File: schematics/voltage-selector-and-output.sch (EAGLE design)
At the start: 24 parts, among them IC2 Tiny85-20-SMT, IC3 MCP41010P, IC4 5V, IC5 MIC2941, X1 USB-A-H

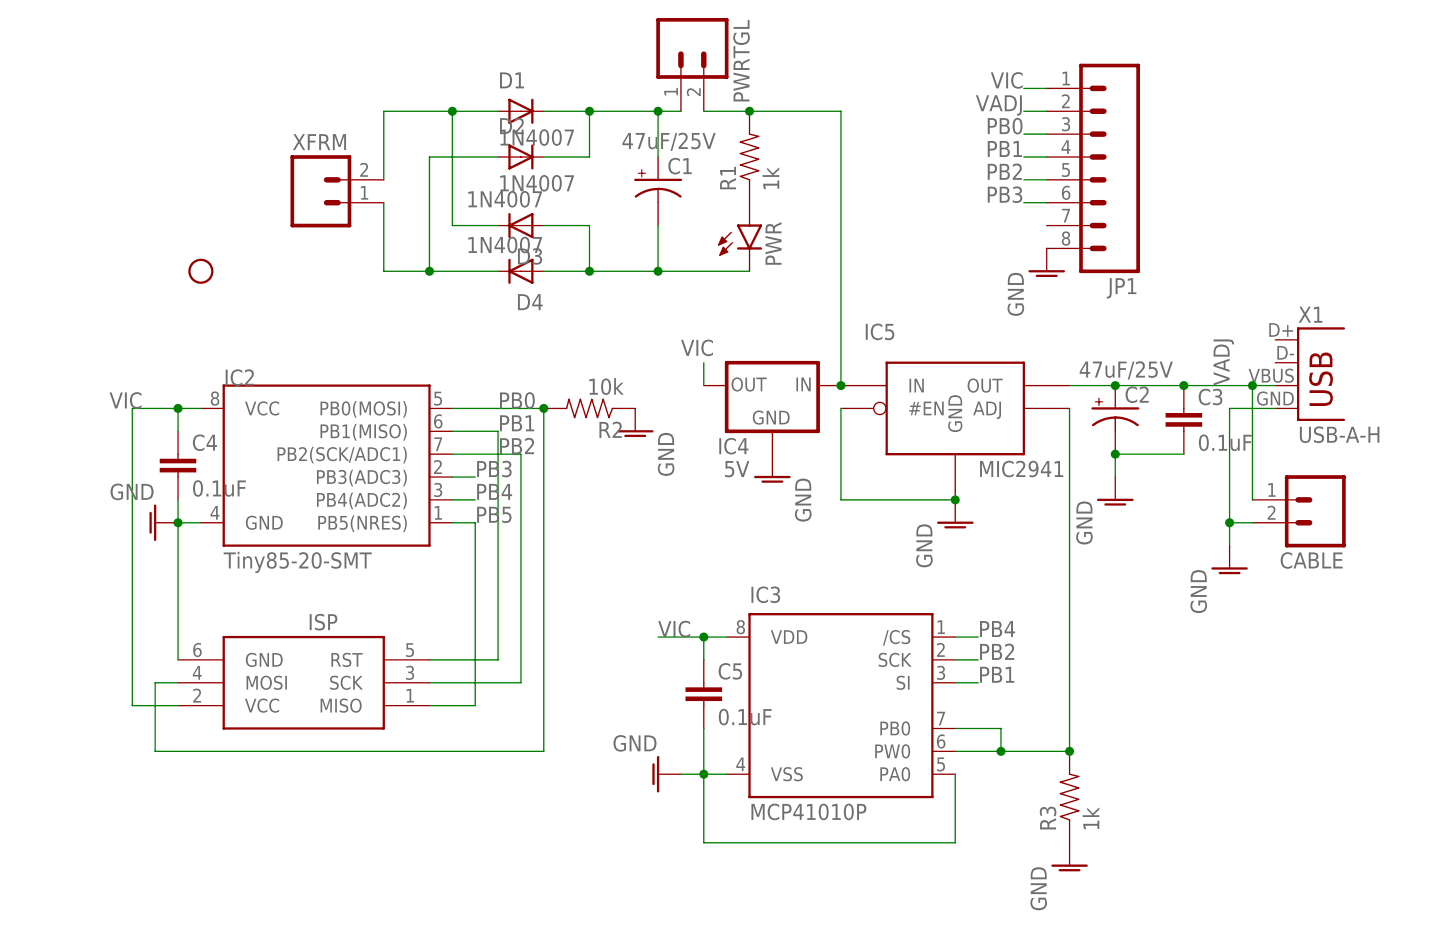
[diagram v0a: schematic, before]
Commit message: Added capacitor for the 5v reg
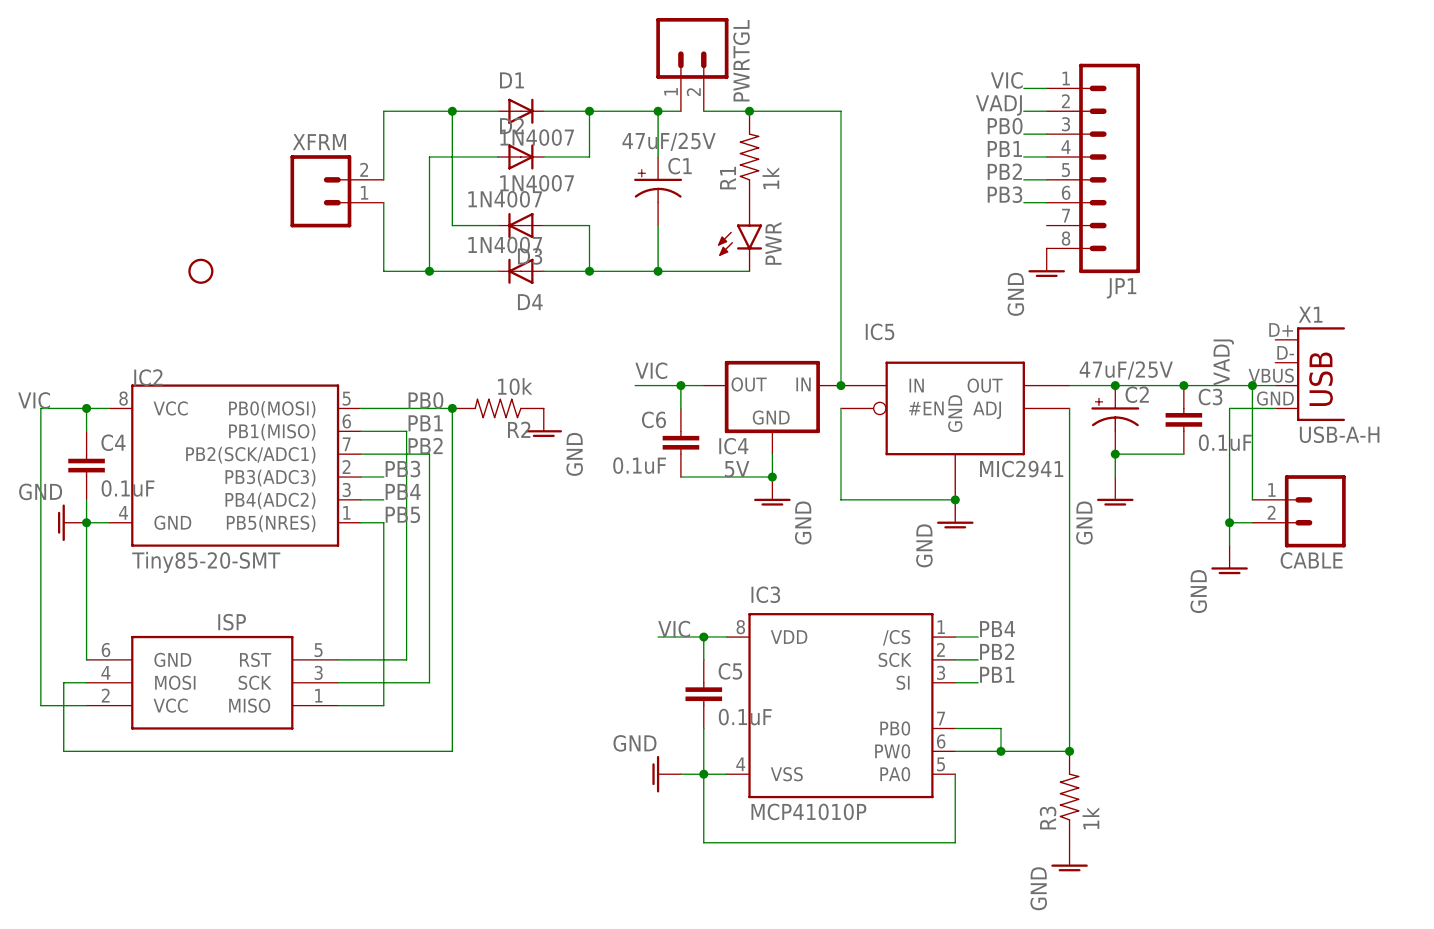
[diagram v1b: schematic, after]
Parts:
- added C6: 0.1uF, SparkFun-Capacitors:1.0UF-25V-+80/-20(0805)"
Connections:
- net AGND: now also C6.2
- net VIC: now also C6.1
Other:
- moved on the sheet: C4, IC2, ISP, R2
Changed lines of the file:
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@@
 <part name="D4" library="diode" deviceset="GF1" device="" value="1N4007"/>
 <part name="IC2" library="SparkFun-DigitalIC" deviceset="ATTINY45" device="TINY85-20-SMT" value="Tiny85-20-SMT"/>
+<part name="C6" library="SparkFun-Capacitors" deviceset="1.0UF-25V-+80/-20(0805)" device="&quot;" value="0.1uF"/>
 </parts>
 <sheets>
@@
 <instance part="CLONE" gate="VR1" x="60.96" y="134.62"/>
 <instance part="GND4" gate="VR1" x="78.74" y="167.64"/>
-<instance part="GND5" gate="VR1" x="27.94" y="177.8" rot="MR0"/>
-<instance part="GND8" gate="VR1" x="12.7" y="182.88" rot="MR0"/>
+<instance part="GND5" gate="VR1" x="27.94" y="175.26" rot="MR0"/>
+<instance part="GND8" gate="VR1" x="2.54" y="182.88" rot="MR0"/>
 <instance part="JP1" gate="G$1" x="63.5" y="213.36" rot="R180"/>
 <instance part="GND7" gate="VR1" x="58.42" y="200.66"/>
 <instance part="IC4" gate="1" x="27.94" y="187.96" rot="MR0"/>
 <instance part="IC3" gate="P1" x="35.56" y="152.4"/>
-<instance part="ISP" gate="G$1" x="-22.86" y="154.94" rot="R180"/>
-<instance part="GND3" gate="VR1" x="-40.64" y="172.72" rot="R270"/>
+<instance part="ISP" gate="G$1" x="-33.02" y="154.94" rot="R180"/>
+<instance part="GND3" gate="VR1" x="-50.8" y="172.72" rot="R270"/>
 <instance part="GND6" gate="VR1" x="15.24" y="144.78" rot="R270"/>
 <instance part="C1" gate="G$1" x="15.24" y="210.82" smashed="yes">
@@
 <instance part="C5" gate="G$1" x="20.32" y="152.4"/>
 <instance part="C3" gate="G$1" x="73.66" y="182.88"/>
-<instance part="C4" gate="G$1" x="-38.1" y="177.8"/>
+<instance part="C4" gate="G$1" x="-48.26" y="177.8"/>
 <instance part="R1" gate="G$1" x="25.4" y="213.36" rot="R90"/>
-<instance part="R2" gate="G$1" x="7.62" y="185.42" rot="R180"/>
+<instance part="R2" gate="G$1" x="-2.54" y="185.42" rot="R180"/>
 <instance part="R3" gate="G$1" x="60.96" y="142.24" rot="R90"/>
 <instance part="D1" gate="D" x="0" y="218.44"/>
@@
 <instance part="D3" gate="D" x="0" y="205.74" rot="R180"/>
 <instance part="D4" gate="D" x="0" y="200.66" rot="R180"/>
-<instance part="IC2" gate="G$1" x="-20.32" y="177.8"/>
+<instance part="IC2" gate="G$1" x="-30.48" y="177.8"/>
+<instance part="C6" gate="G$1" x="17.78" y="180.34" rot="MR0"/>
 </instances>
 <busses>
@@
 <segment>
 <pinref part="IC4" gate="1" pin="OUT"/>
-<wire x1="20.32" y1="187.96" x2="20.32" y2="190.5" width="0.1524" layer="91"/>
-<label x="17.78" y="193.04" size="1.778" layer="95" rot="MR180"/>
-</segment>
-<segment>
-<label x="-45.72" y="185.42" size="1.778" layer="95"/>
+<wire x1="20.32" y1="187.96" x2="17.78" y2="187.96" width="0.1524" layer="91"/>
+<label x="12.7" y="190.5" size="1.778" layer="95" rot="MR180"/>
+<junction x="17.78" y="187.96"/>
+<wire x1="17.78" y1="187.96" x2="12.7" y2="187.96" width="0.1524" layer="91"/>
+<pinref part="C6" gate="G$1" pin="1"/>
+<wire x1="17.78" y1="187.96" x2="17.78" y2="185.42" width="0.1524" layer="91"/>
+</segment>
+<segment>
+<label x="-55.88" y="185.42" size="1.778" layer="95"/>
 <pinref part="ISP" gate="G$1" pin="VCC"/>
-<wire x1="-38.1" y1="152.4" x2="-43.18" y2="152.4" width="0.1524" layer="91"/>
-<wire x1="-43.18" y1="152.4" x2="-43.18" y2="185.42" width="0.1524" layer="91"/>
-<wire x1="-43.18" y1="185.42" x2="-38.1" y2="185.42" width="0.1524" layer="91"/>
-<junction x="-38.1" y="185.42"/>
-<wire x1="-38.1" y1="185.42" x2="-35.56" y2="185.42" width="0.1524" layer="91"/>
-<wire x1="-38.1" y1="182.88" x2="-38.1" y2="185.42" width="0.1524" layer="91"/>
+<wire x1="-48.26" y1="152.4" x2="-53.34" y2="152.4" width="0.1524" layer="91"/>
+<wire x1="-53.34" y1="152.4" x2="-53.34" y2="185.42" width="0.1524" layer="91"/>
+<wire x1="-53.34" y1="185.42" x2="-48.26" y2="185.42" width="0.1524" layer="91"/>
+<junction x="-48.26" y="185.42"/>
+<wire x1="-48.26" y1="185.42" x2="-45.72" y2="185.42" width="0.1524" layer="91"/>
+<wire x1="-48.26" y1="182.88" x2="-48.26" y2="185.42" width="0.1524" layer="91"/>
 <pinref part="C4" gate="G$1" pin="1"/>
 <pinref part="IC2" gate="G$1" pin="VCC"/>
@@
 <segment>
 <pinref part="ISP" gate="G$1" pin="MISO"/>
-<wire x1="-10.16" y1="152.4" x2="-5.08" y2="152.4" width="0.1524" layer="91"/>
-<wire x1="-7.62" y1="172.72" x2="-5.08" y2="172.72" width="0.1524" layer="91"/>
-<wire x1="-5.08" y1="152.4" x2="-5.08" y2="172.72" width="0.1524" layer="91"/>
-<label x="-5.08" y="172.72" size="1.778" layer="95"/>
+<wire x1="-20.32" y1="152.4" x2="-15.24" y2="152.4" width="0.1524" layer="91"/>
+<wire x1="-17.78" y1="172.72" x2="-15.24" y2="172.72" width="0.1524" layer="91"/>
+<wire x1="-15.24" y1="152.4" x2="-15.24" y2="172.72" width="0.1524" layer="91"/>
+<label x="-15.24" y="172.72" size="1.778" layer="95"/>
 <pinref part="IC2" gate="G$1" pin="PB5(NRES)"/>
 </segment>
@@
 <net name="PB2" class="0">
 <segment>
-<wire x1="0" y1="180.34" x2="-7.62" y2="180.34" width="0.1524" layer="91"/>
+<wire x1="-10.16" y1="180.34" x2="-17.78" y2="180.34" width="0.1524" layer="91"/>
 <pinref part="ISP" gate="G$1" pin="SCK"/>
-<wire x1="-10.16" y1="154.94" x2="0" y2="154.94" width="0.1524" layer="91"/>
-<wire x1="0" y1="154.94" x2="0" y2="180.34" width="0.1524" layer="91"/>
-<label x="-2.54" y="180.34" size="1.778" layer="95"/>
+<wire x1="-20.32" y1="154.94" x2="-10.16" y2="154.94" width="0.1524" layer="91"/>
+<wire x1="-10.16" y1="154.94" x2="-10.16" y2="180.34" width="0.1524" layer="91"/>
+<label x="-12.7" y="180.34" size="1.778" layer="95"/>
 <pinref part="IC2" gate="G$1" pin="PB2(SCK/ADC1)"/>
 </segment>
@@
 <net name="PB1" class="0">
 <segment>
-<wire x1="-2.54" y1="182.88" x2="-7.62" y2="182.88" width="0.1524" layer="91"/>
+<wire x1="-12.7" y1="182.88" x2="-17.78" y2="182.88" width="0.1524" layer="91"/>
 <pinref part="ISP" gate="G$1" pin="RST"/>
-<wire x1="-10.16" y1="157.48" x2="-2.54" y2="157.48" width="0.1524" layer="91"/>
-<wire x1="-2.54" y1="157.48" x2="-2.54" y2="182.88" width="0.1524" layer="91"/>
-<label x="-2.54" y="182.88" size="1.778" layer="95"/>
+<wire x1="-20.32" y1="157.48" x2="-12.7" y2="157.48" width="0.1524" layer="91"/>
+<wire x1="-12.7" y1="157.48" x2="-12.7" y2="182.88" width="0.1524" layer="91"/>
+<label x="-12.7" y="182.88" size="1.778" layer="95"/>
 <pinref part="IC2" gate="G$1" pin="PB1(MISO)"/>
 </segment>
@@
 <net name="PB3" class="0">
 <segment>
-<wire x1="-7.62" y1="177.8" x2="-5.08" y2="177.8" width="0.1524" layer="91"/>
-<label x="-5.08" y="177.8" size="1.778" layer="95"/>
+<wire x1="-17.78" y1="177.8" x2="-15.24" y2="177.8" width="0.1524" layer="91"/>
+<label x="-15.24" y="177.8" size="1.778" layer="95"/>
 <pinref part="IC2" gate="G$1" pin="PB3(ADC3)"/>
 </segment>
@@
 <net name="PB4" class="0">
 <segment>
-<wire x1="-7.62" y1="175.26" x2="-5.08" y2="175.26" width="0.1524" layer="91"/>
-<label x="-5.08" y="175.26" size="1.778" layer="95"/>
+<wire x1="-17.78" y1="175.26" x2="-15.24" y2="175.26" width="0.1524" layer="91"/>
+<label x="-15.24" y="175.26" size="1.778" layer="95"/>
 <pinref part="IC2" gate="G$1" pin="PB4(ADC2)"/>
 </segment>
@@
 <net name="PB0" class="0">
 <segment>
-<wire x1="2.54" y1="185.42" x2="-7.62" y2="185.42" width="0.1524" layer="91"/>
+<wire x1="-7.62" y1="185.42" x2="-17.78" y2="185.42" width="0.1524" layer="91"/>
 <pinref part="ISP" gate="G$1" pin="MOSI"/>
-<wire x1="-38.1" y1="154.94" x2="-40.64" y2="154.94" width="0.1524" layer="91"/>
-<wire x1="-40.64" y1="154.94" x2="-40.64" y2="147.32" width="0.1524" layer="91"/>
-<wire x1="-40.64" y1="147.32" x2="2.54" y2="147.32" width="0.1524" layer="91"/>
-<wire x1="2.54" y1="147.32" x2="2.54" y2="185.42" width="0.1524" layer="91"/>
-<label x="-2.54" y="185.42" size="1.778" layer="95"/>
+<wire x1="-48.26" y1="154.94" x2="-50.8" y2="154.94" width="0.1524" layer="91"/>
+<wire x1="-50.8" y1="154.94" x2="-50.8" y2="147.32" width="0.1524" layer="91"/>
+<wire x1="-50.8" y1="147.32" x2="-7.62" y2="147.32" width="0.1524" layer="91"/>
+<wire x1="-7.62" y1="147.32" x2="-7.62" y2="185.42" width="0.1524" layer="91"/>
+<label x="-12.7" y="185.42" size="1.778" layer="95"/>
 <pinref part="R2" gate="G$1" pin="2"/>
-<junction x="2.54" y="185.42"/>
+<junction x="-7.62" y="185.42"/>
 <pinref part="IC2" gate="G$1" pin="PB0(MOSI)"/>
 </segment>
@@
 <segment>
 <pinref part="GND3" gate="VR1" pin="AGND"/>
-<wire x1="-35.56" y1="172.72" x2="-38.1" y2="172.72" width="0.1524" layer="91"/>
+<wire x1="-45.72" y1="172.72" x2="-48.26" y2="172.72" width="0.1524" layer="91"/>
 <pinref part="ISP" gate="G$1" pin="GND"/>
-<wire x1="-38.1" y1="157.48" x2="-38.1" y2="172.72" width="0.1524" layer="91"/>
-<junction x="-38.1" y="172.72"/>
-<wire x1="-38.1" y1="175.26" x2="-38.1" y2="172.72" width="0.1524" layer="91"/>
+<wire x1="-48.26" y1="157.48" x2="-48.26" y2="172.72" width="0.1524" layer="91"/>
+<junction x="-48.26" y="172.72"/>
+<wire x1="-48.26" y1="175.26" x2="-48.26" y2="172.72" width="0.1524" layer="91"/>
 <pinref part="C4" gate="G$1" pin="2"/>
 <pinref part="IC2" gate="G$1" pin="GND"/>
@@
 <pinref part="IC4" gate="1" pin="GND"/>
 <pinref part="GND5" gate="VR1" pin="AGND"/>
-</segment>
-<segment>
+<wire x1="27.94" y1="177.8" x2="27.94" y2="180.34" width="0.1524" layer="91"/>
+<pinref part="C6" gate="G$1" pin="2"/>
+<wire x1="27.94" y1="177.8" x2="17.78" y2="177.8" width="0.1524" layer="91"/>
+<junction x="27.94" y="177.8"/>
+</segment>
+<segment>
